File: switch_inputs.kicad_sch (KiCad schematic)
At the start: 20 parts, among them U12 PRTR5V0U2X, U13 PRTR5V0U2X, U14 PRTR5V0U2X, U15 PRTR5V0U2X

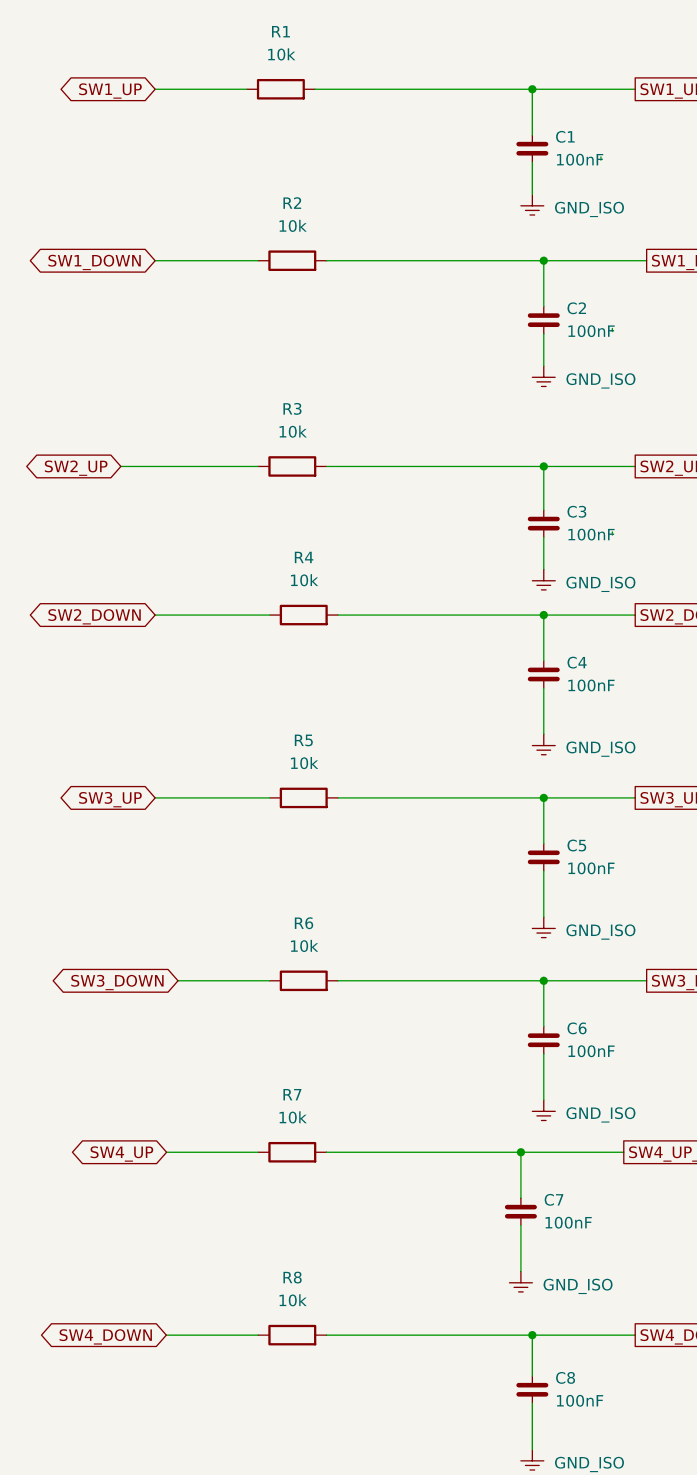
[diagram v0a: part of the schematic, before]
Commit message: Pre-fab QA review fixes: switch input levels, power path, sensor spec, ESD
- R1-R8 switch series resistors 10k -> 1k: with only the ESP32 internal
  ~45k pull-up, 10k divided a closed switch to 0.6V vs the S3's 0.825V
  VIL limit — marginal. 1k gives ~0.1-0.23V worst case.
- U11 ACS723 -> ACS725LLCTR-05AB-T (C3684552): ACS723 needs 4.5-5.5V but
  ran at 3.3V (out of spec). ACS725 is 3.3V-native, same SOIC-8, rated
  to +150C. Firmware: sensitivity 264mV/A, formula (x-1.65)/0.264.
- D2 BAT54C (200mA) removed; replaced with D10/D11 SS34 (3A) diode-OR.
  The old diode carried the full ESP32 load permanently; WiFi TX bursts
  reach 350-500mA.
- U16 PRTR5V0U2X added on USB D+/D- (ESD protection at J2).
- D1 SS34 -> SS54 (5A, same SMA footprint) for multi-motor headroom.
- C10 bumped to 25V-rated 100uF 1210 (C2840614), same footprint.
- Filled all missing LCSC fields for JLCPCB assembly BOM.
- Docs: J4 pinout corrected to as-built; firmware bring-up checklist and
  RTS/DTR terminal gotcha added; CLAUDE.md placement guide for D10/D11/U16.

PCB placement of D10/D11/U16 + F8 sync still pending.

Co-Authored-By: Claude Fable 5 <noreply@anthropic.com>
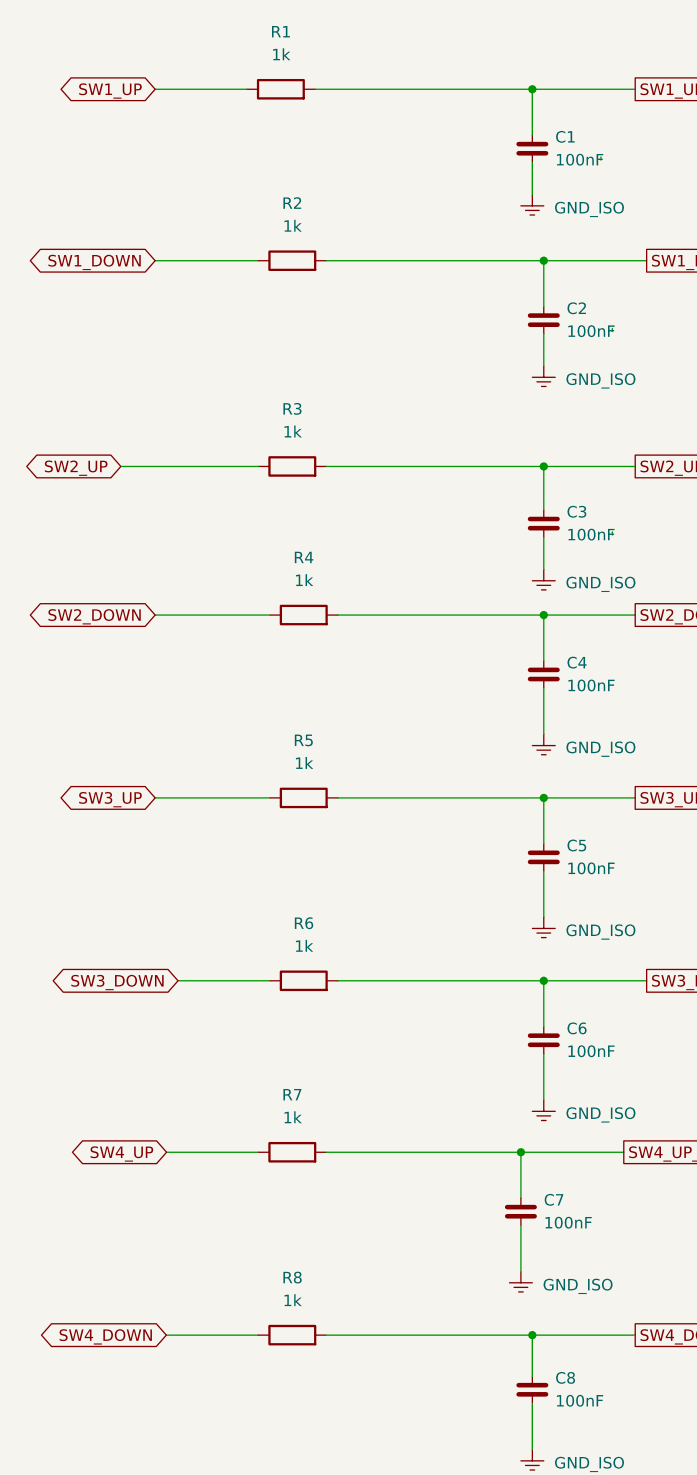
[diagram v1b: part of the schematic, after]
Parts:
- C1, C2, C3, C4, C5, C6, C7, C8: LCSC (none) -> C1525
- R1, R2, R3, R4, R5, R6, R7, R8: value 10k -> 1k
- U12, U13, U14, U15: LCSC (none) -> C12333
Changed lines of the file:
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@@
+			)
+		)
+		(property "LCSC" "C1525"
+			(at 86.36 52.324 0)
+			(hide yes)
+			(show_name no)
+			(do_not_autoplace no)
+			(effects
+				(font
+					(size 1.27 1.27)
+				)
 			)
 		)
@@
 			)
 		)
+		(property "LCSC" "C1525"
+			(at 85.09 171.17 0)
+			(hide yes)
+			(show_name no)
+			(do_not_autoplace no)
+			(effects
+				(font
+					(size 1.27 1.27)
+				)
+			)
+		)
 		(pin "1"
 		)
@@
 			)
 		)
-		(property "Value" "10k"
+		(property "Value" "1k"
 			(at 58.42 64.77 90)
 			(show_name no)
@@
 			)
 		)
+		(property "LCSC" "C1525"
+			(at 86.36 74.93 0)
+			(hide yes)
+			(show_name no)
+			(do_not_autoplace no)
+			(effects
+				(font
+					(size 1.27 1.27)
+				)
+			)
+		)
 		(pin "1"
 		)
@@
 			)
 		)
+		(property "LCSC" "C1525"
+			(at 86.36 91.694 0)
+			(hide yes)
+			(show_name no)
+			(do_not_autoplace no)
+			(effects
+				(font
+					(size 1.27 1.27)
+				)
+			)
+		)
 		(pin "1"
 		)
@@
 			)
 		)
+		(property "LCSC" "C12333"
+			(at 135.89 33.02 0)
+			(hide yes)
+			(show_name no)
+			(do_not_autoplace no)
+			(effects
+				(font
+					(size 1.27 1.27)
+				)
+			)
+		)
 		(pin "1"
 		)
@@
 		)
 		(property "Description" "Ultra low capacitance double rail-to-rail ESD protection diode, SOT-143"
+			(at 133.35 152.4 0)
+			(hide yes)
+			(show_name no)
+			(do_not_autoplace no)
+			(effects
+				(font
+					(size 1.27 1.27)
+				)
+			)
+		)
+		(property "LCSC" "C12333"
 			(at 133.35 152.4 0)
 			(hide yes)
@@
 			)
 		)
+		(property "LCSC" "C1525"
+			(at 86.36 112.014 0)
+			(hide yes)
+			(show_name no)
+			(do_not_autoplace no)
+			(effects
+				(font
+					(size 1.27 1.27)
+				)
+			)
+		)
 		(pin "1"
 		)
@@
 			)
 		)
+		(property "LCSC" "C12333"
+			(at 135.89 76.2 0)
+			(hide yes)
+			(show_name no)
+			(do_not_autoplace no)
+			(effects
+				(font
+					(size 1.27 1.27)
+				)
+			)
+		)
 		(pin "1"
 		)
@@
 			)
 		)
+		(property "LCSC" "C1525"
+			(at 83.82 151.384 0)
+			(hide yes)
+			(show_name no)
+			(do_not_autoplace no)
+			(effects
+				(font
+					(size 1.27 1.27)
+				)
+			)
+		)
 		(pin "1"
 		)
@@
 			)
 		)
-		(property "Value" "10k"
+		(property "Value" "1k"
 			(at 58.42 41.91 90)
 			(show_name no)
@@
 			)
 		)
+		(property "LCSC" "C1525"
+			(at 85.09 33.274 0)
+			(hide yes)
+			(show_name no)
+			(do_not_autoplace no)
+			(effects
+				(font
+					(size 1.27 1.27)
+				)
+			)
+		)
 		(pin "1"
 		)
@@
 			)
 		)
-		(property "Value" "10k"
+		(property "Value" "1k"
 			(at 59.69 121.92 90)
 			(show_name no)
@@
 			)
 		)
-		(property "Value" "10k"
+		(property "Value" "1k"
 			(at 59.69 81.28 90)
 			(show_name no)
@@
 		)
 		(property "Description" "Ultra low capacitance double rail-to-rail ESD protection diode, SOT-143"
+			(at 133.35 111.76 0)
+			(hide yes)
+			(show_name no)
+			(do_not_autoplace no)
+			(effects
+				(font
+					(size 1.27 1.27)
+				)
+			)
+		)
+		(property "LCSC" "C12333"
 			(at 133.35 111.76 0)
 			(hide yes)
@@
 			)
 		)
-		(property "Value" "10k"
+		(property "Value" "1k"
 			(at 58.42 140.97 90)
 			(show_name no)
@@
 			)
 		)
+		(property "LCSC" "C1525"
+			(at 86.36 132.334 0)
+			(hide yes)
+			(show_name no)
+			(do_not_autoplace no)
+			(effects
+				(font
+					(size 1.27 1.27)
+				)
+			)
+		)
 		(pin "1"
 		)
@@
 			)
 		)
-		(property "Value" "10k"
+		(property "Value" "1k"
 			(at 59.69 101.6 90)
 			(show_name no)
@@
 			)
 		)
-		(property "Value" "10k"
+		(property "Value" "1k"
 			(at 57.15 22.86 90)
 			(show_name no)
@@
 			)
 		)
-		(property "Value" "10k"
+		(property "Value" "1k"
 			(at 58.42 161.29 90)
 			(show_name no)

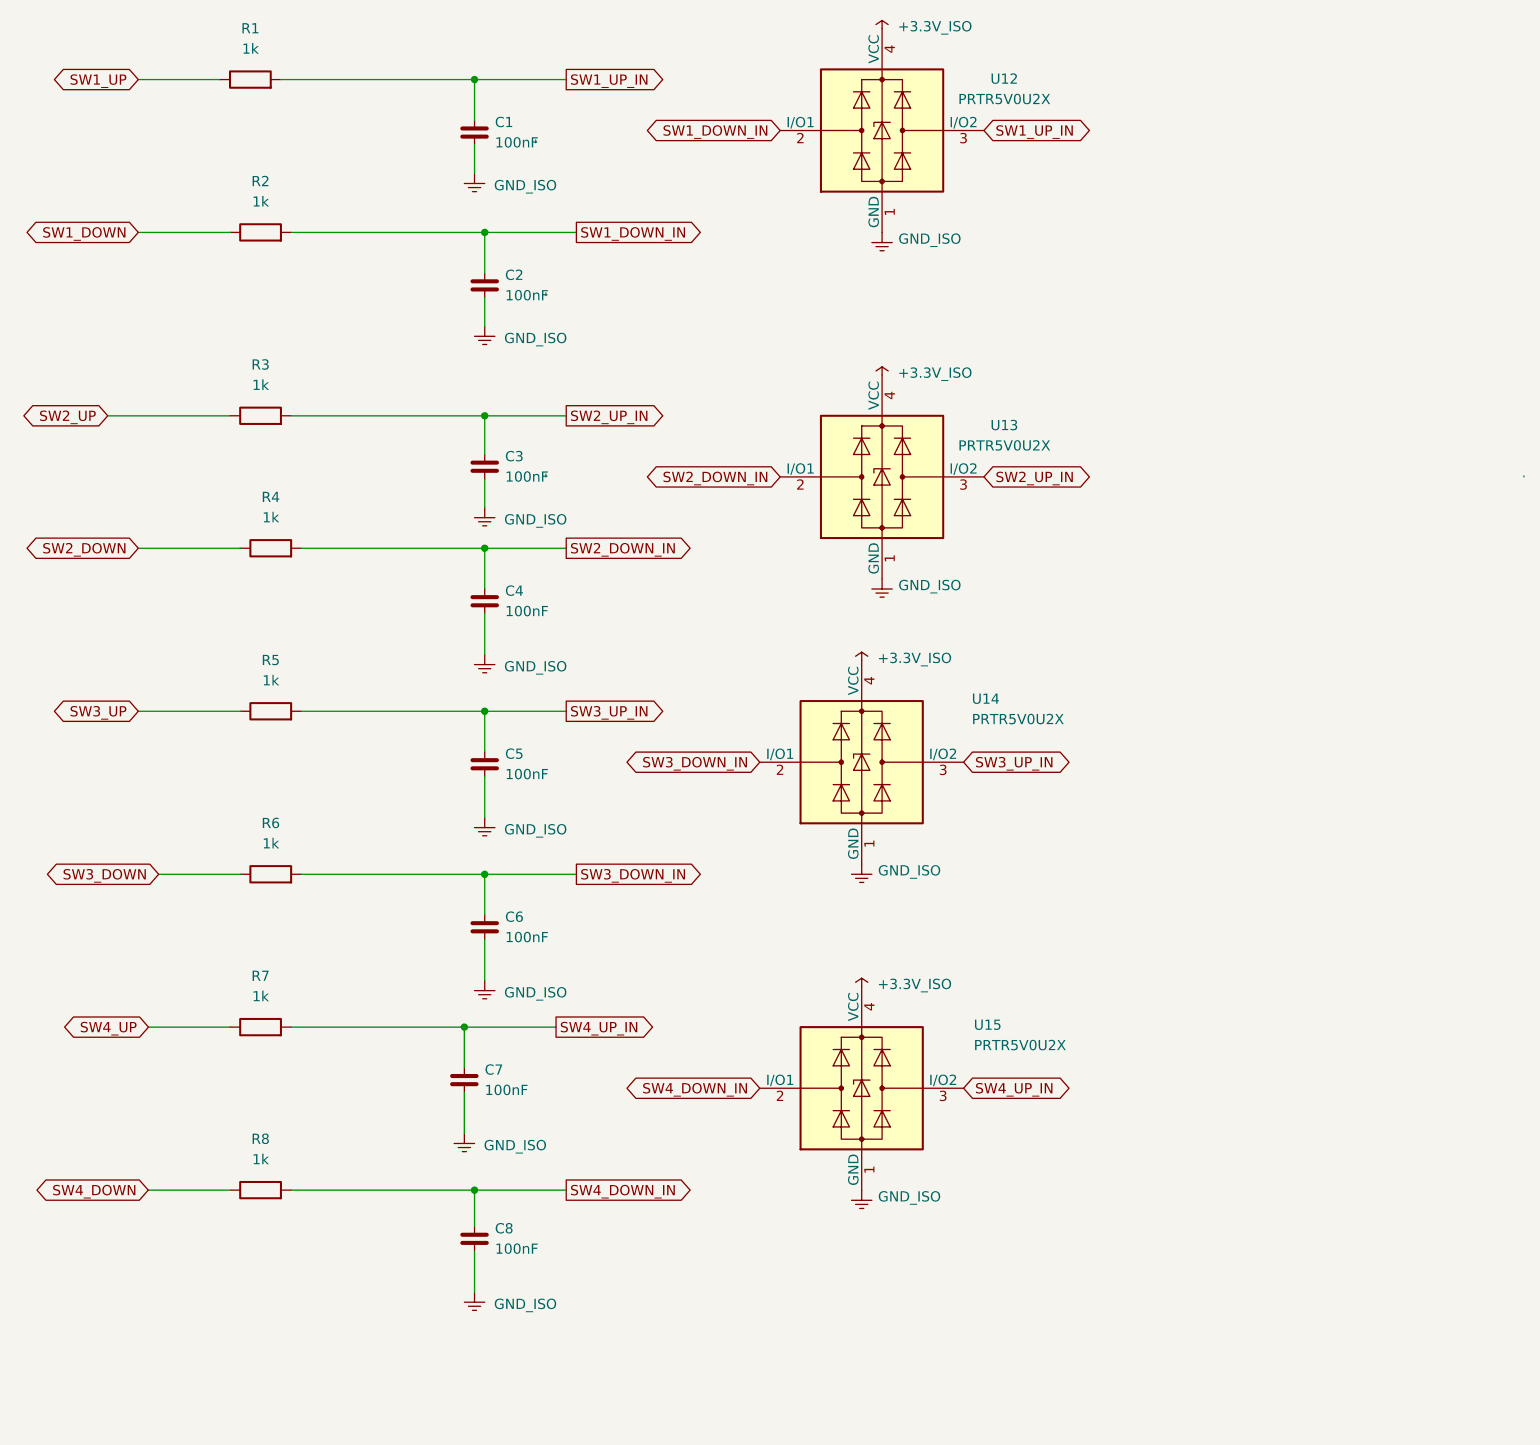
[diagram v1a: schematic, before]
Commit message: Rev 1.3 PCB sync + second QA pass: BOM fixes, TVS decoupling, ERC cleanup
PCB (done in KiCad, verified here):
- F8 sync applied: D2 removed; D10/D11 (SS34 SMA) and U16 (PRTR5V0U2X SOT-143)
  placed and routed; R1-R8 -> 1k, D1 -> SS54, C10 -> 25V, U11 -> ACS725 updated
  in place. Footprint-level diff confirms exactly the intended delta, nothing
  else moved. DRC 0 errors / 0 unconnected pads.

Schematic fixes from the second QA pass:
- R1-R8 had NO LCSC part number (value change had landed, part number never
  did) - they would have come back unpopulated, silently killing the switch
  inputs. Set to C14676, matching R14's existing 1K 0603 so it consolidates to
  one BOM line. NOTE: todo.md originally specified C21190 - see the discrepancy
  note there and confirm before ordering.
- TP1-TP7 set in_bom no / in_pos_files no (were 7 junk lines in the JLCPCB BOM).
- Removed 4 orphan dangling wire stubs in switch_inputs.kicad_sch.
- Converted the orphan STBY hierarchical label in motor_drivers.kicad_sch to a
  global label rather than deleting it: its wire actually carried U9 pin 19, so
  deleting dropped U9.19 off the STBY net. Converting keeps the connection and
  clears the ERC hier_label_mismatch.
- Added C40-C43 (100nF 0402, C1525) for U12-U15 VCC decoupling. The switch-input
  TVS devices currently have their nearest +3.3V_ISO bypass 18-23mm away; a
  PRTR5V0U2X shunts ESD into VCC and needs somewhere local to dump it. Still
  need PCB placement - put each within ~2mm of its device's pin 4.

Every schematic edit was validated by diffing the exported netlist before and
after; connectivity is unchanged apart from the four intended new caps.
ERC errors: 10 -> 5 (remaining are 4x missing PWR_FLAG and one J2-GND/U1-(-Vout)
both-power-output pair that is correct by design).

Added barn-blinds-controller.kicad_dru: isolation-barrier audit rule. The board
has no dedicated ISO/MOTOR gap - minimum copper spacing between domains is
0.20mm, the global default. Rev 1.2 measured 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
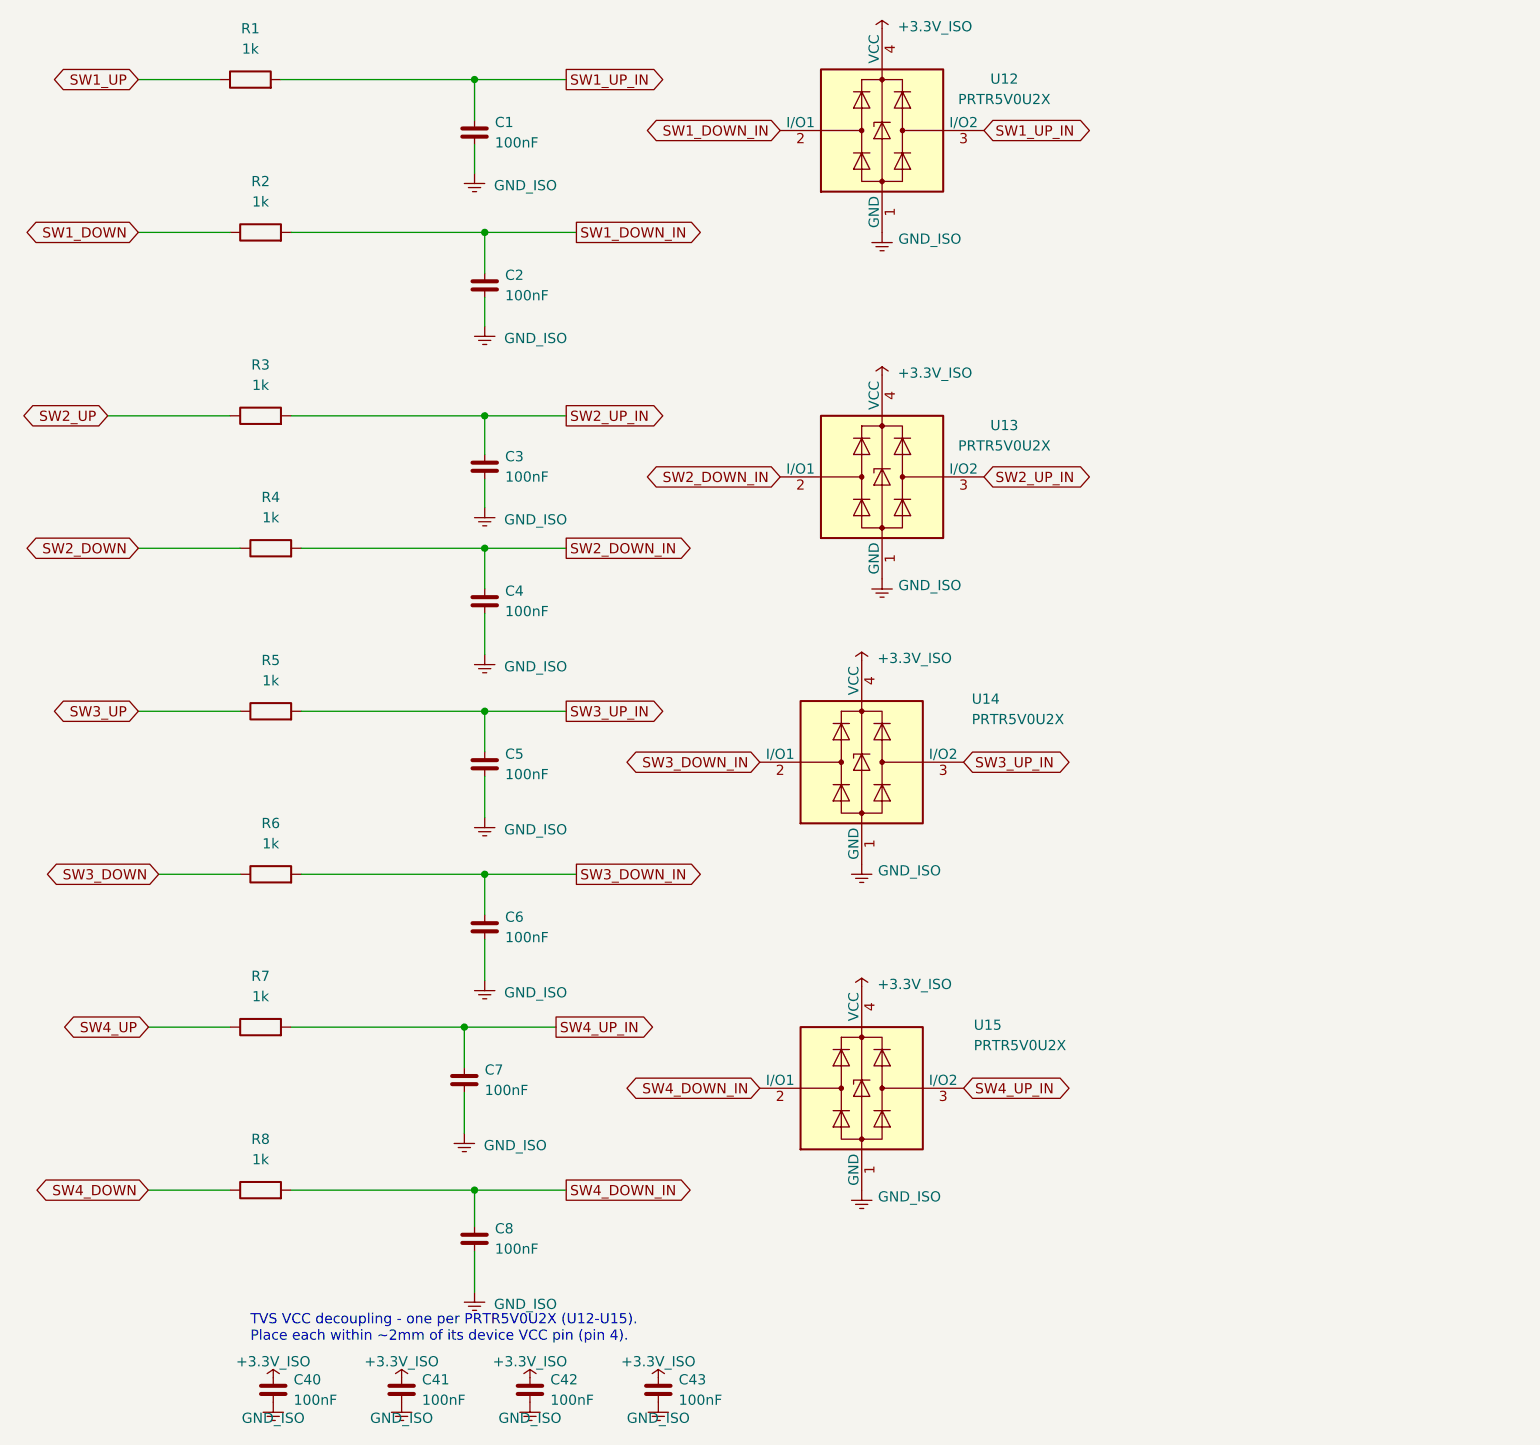
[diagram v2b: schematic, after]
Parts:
- added C40, C41, C42, C43: 100nF, Capacitor_SMD:C_0402_1005Metric, symbol Device:C
- R1, R2, R3, R4, R5, R6, R7, R8: LCSC (none) -> C14676
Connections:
- net +3.3V_ISO: now also C40.1, C41.1, C42.1, C43.1
- net GND_ISO: now also C40.2, C41.2, C42.2, C43.2
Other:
- note added: "TVS VCC decoupling - one per PRTR5V0U2X (U12-U15). Place each within ~2mm of its device VCC pin (pin 4)."
